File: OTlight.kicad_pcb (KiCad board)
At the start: 2 copper layers, 58 parts, among them P1 CONN_01X01, Q1 TEMT6000, Q2 Q_NMOS_GSD, T1 TRANSFO, U1 LM3478, U10 IN-14, U11 IN-14, U12 MAX6931, U13 IN-14, U14 MAX6920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

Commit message: Components fitted
Everything fits!
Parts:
- added C1: 220u, Capacitors_SMD:CP_Elec_6.3x7.7, F.Cu at (65.5, 127.6)
- added D1: STPS4S200, Diodes_SMD:D_SMB_Handsoldering, F.Cu at (48.3, 91.9)
- added U3: DS3231, BamboulabFootprints:DS3231, F.Cu at (128.5, 58.9)
- added U7: BME280, BamboulabFootprints:BME280, F.Cu at (98.1, 62.6)
- P1: footprint Connect:1pin -> Socket_Strips:Socket_Strip_Straight_1x01_Pitch2.54mm
- moved R24 202.0 mm to (54.9, 92.1), turned to 90 degrees
- moved C5 197.0 mm to (52.3, 128.0), turned to 270 degrees
- moved C6 193.8 mm to (78.5, 114.8)
- moved C4 189.6 mm to (58.9, 128.0), turned to 270 degrees
- moved R8 188.8 mm to (55.4, 128.0), turned to 270 degrees
- moved R1 188.7 mm to (79.8, 123.4)
- moved C2 187.9 mm to (65.0, 120.4), turned to 270 degrees
- moved R17 186.8 mm to (57.4, 92.3), turned to 270 degrees
- moved C3 182.9 mm to (74.7, 123.4)
- moved U1 182.1 mm to (74.2, 118.9), turned to 270 degrees
- moved R2 174.4 mm to (68.1, 120.4), turned to 270 degrees
- moved R4 170.3 mm to (94.0, 120.9), turned to 90 degrees
- moved R25 169.0 mm to (81.8, 91.4), turned to 90 degrees
- moved R28 168.9 mm to (97.5, 91.4), turned to 90 degrees
- moved R23 167.5 mm to (59.9, 91.9), turned to 90 degrees
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
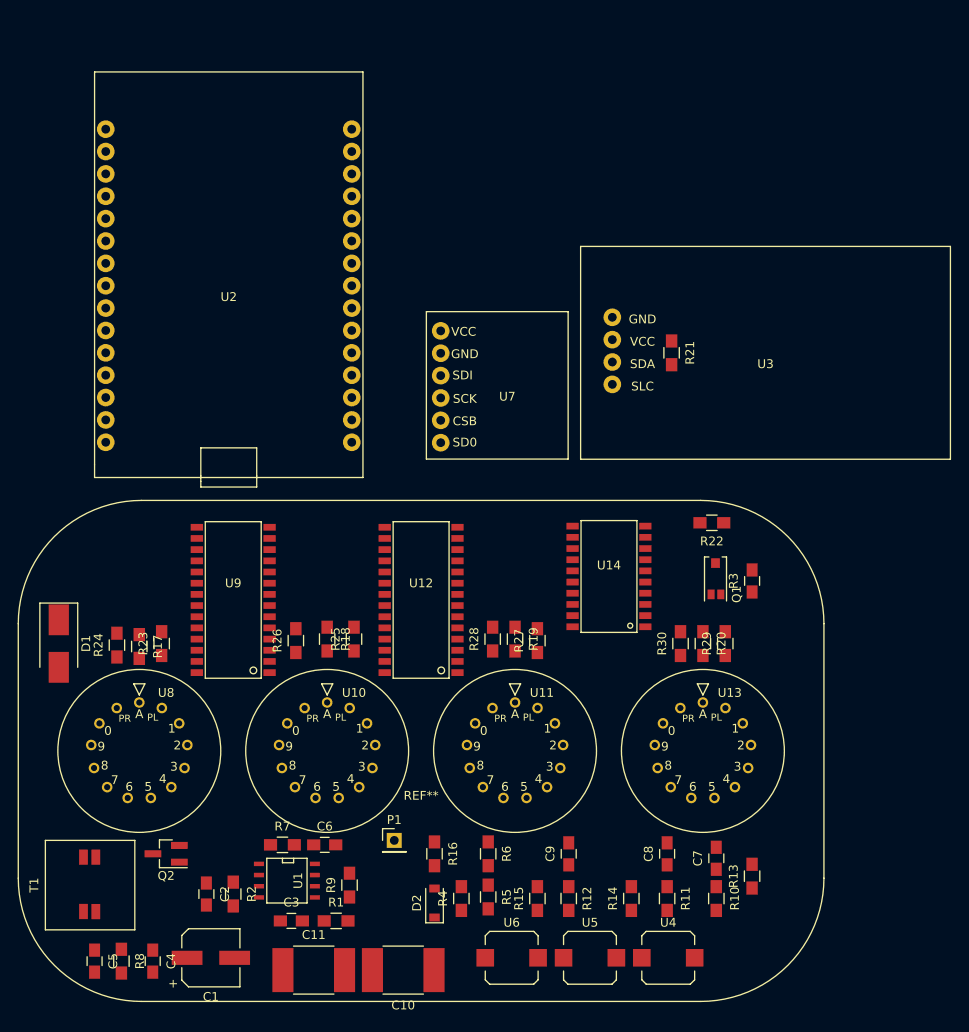
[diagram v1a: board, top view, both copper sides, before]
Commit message: PSU on board organised
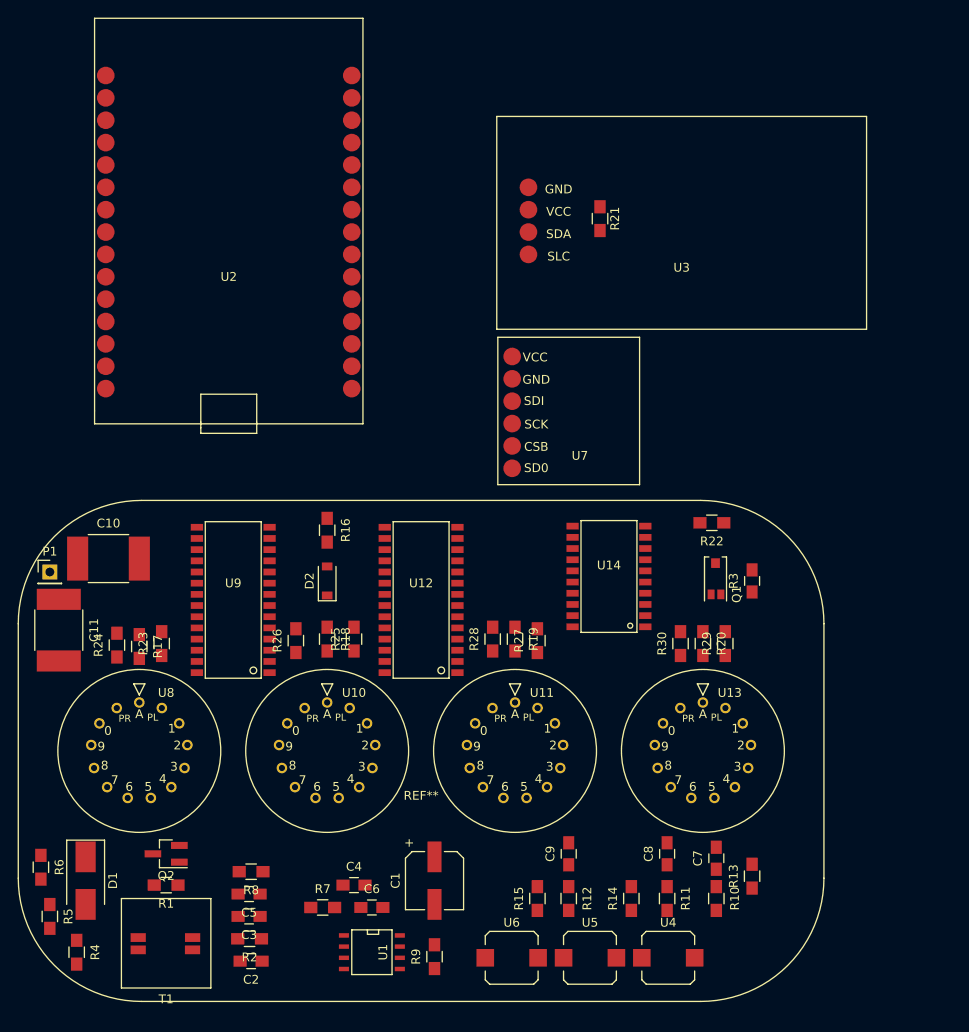
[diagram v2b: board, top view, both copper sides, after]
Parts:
- moved C10 57.5 mm to (53.9, 82.3), turned to 0 degrees
- moved R6 50.8 mm to (46.2, 117.3)
- moved R5 49.8 mm to (47.2, 122.9)
- moved P1 49.6 mm to (47.2, 83.8)
- moved C11 48.3 mm to (48.3, 90.4), turned to 270 degrees
- moved R4 44.1 mm to (50.3, 127.0), turned to 270 degrees
- moved R16 38.7 mm to (78.7, 79.1)
- moved D2 38.6 mm to (78.7, 84.8)
- moved D1 27.1 mm to (51.3, 118.9)
- moved C1 26.9 mm to (90.9, 118.9), turned to 270 degrees
- moved C4 24.4 mm to (81.8, 119.4), turned to 0 degrees
- moved R1 19.7 mm to (60.5, 119.4), turned to 180 degrees
- moved C5 19.1 mm to (69.9, 120.4), turned to 180 degrees
- moved R8 17.9 mm to (70.1, 117.9), turned to 180 degrees
- moved U3 17.6 mm to (119.0, 44.2)
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
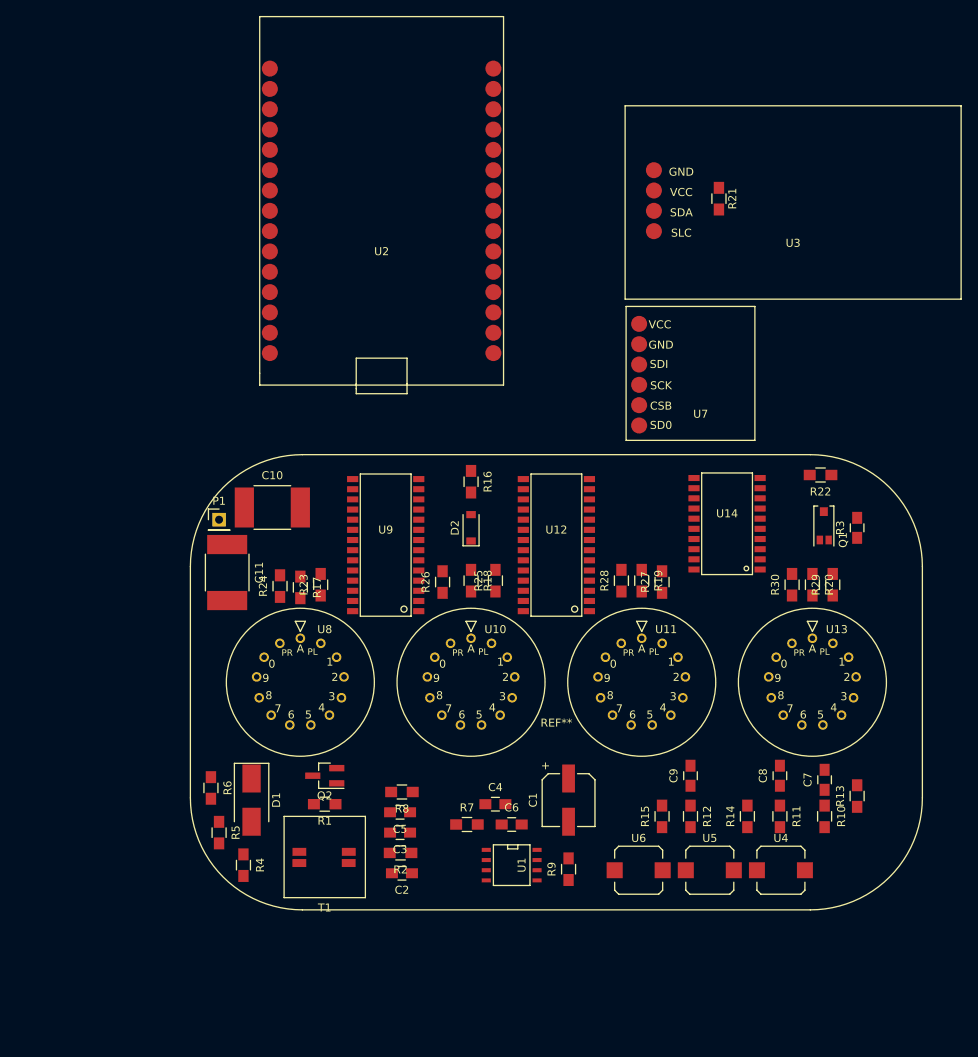
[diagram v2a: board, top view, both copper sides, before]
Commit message: ShiftRegisters + Nixies Routed
ESP in place also
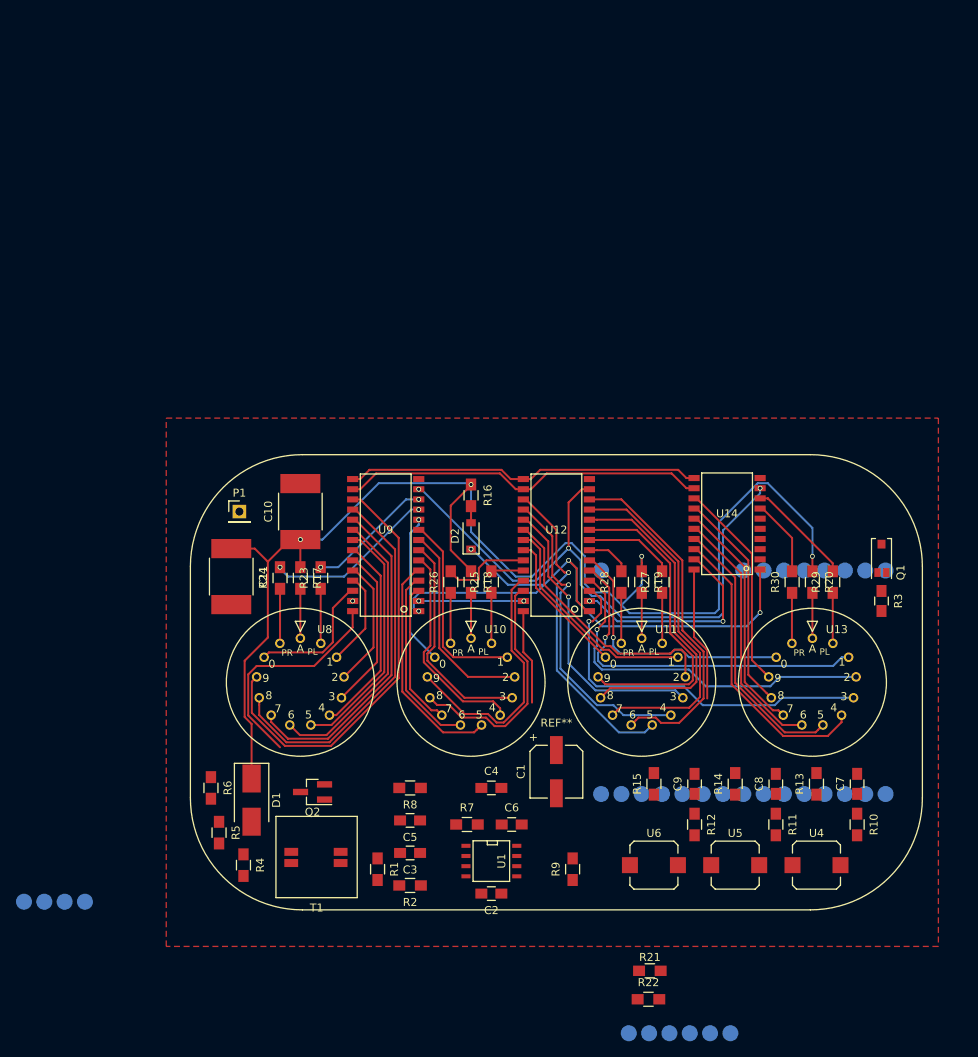
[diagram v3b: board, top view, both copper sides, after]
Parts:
- U2, U3, U7: moved to B.Cu
- moved U3 116.0 mm to (26.4, 114.2), turned to 90 degrees
- moved R21 96.9 mm to (101.1, 140.2), turned to 0 degrees
- moved U7 88.9 mm to (104.6, 154.4), turned to 270 degrees
- moved U2 74.3 mm to (112.8, 104.1), turned to 270 degrees
- moved R22 69.0 mm to (100.9, 143.8), turned to 0 degrees
- moved C2 11.5 mm to (81.3, 130.6)
- moved R1 10.5 mm to (67.1, 127.5), turned to 270 degrees
- moved R3 9.64 mm to (130.0, 94.0), turned to 270 degrees
- moved Q1 8.27 mm to (130.0, 90.4)
- moved R13 5.30 mm to (121.9, 116.8)
- moved U4 4.49 mm to (121.9, 127.0)
- moved R14 4.34 mm to (111.8, 116.8)
- moved R2 4.23 mm to (71.1, 129.5)
- moved R10 4.19 mm to (127.0, 121.9)
- moved R15 4.19 mm to (101.6, 116.8)
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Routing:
- net /HVout: track 0.00 -> 168.1 mm, vias 0 -> 4
- net Net-(D2-Pad1): track 0.00 -> 77.8 mm, vias 0 -> 4
- net /BLANK: track 0.00 -> 76.6 mm, vias 0 -> 3
- net +3V3: track 0.00 -> 57.0 mm
- net Net-(U8-Pad11): track 0.00 -> 53.6 mm
- net Net-(U12-Pad3): track 0.00 -> 47.6 mm, vias 0 -> 1
- net Net-(U8-Pad10): track 0.00 -> 47.2 mm
- net Net-(U12-Pad4): track 0.00 -> 46.2 mm, vias 0 -> 1
- net /LOAD: track 0.00 -> 45.9 mm
- net Net-(U12-Pad5): track 0.00 -> 45.5 mm, vias 0 -> 1
- net /CLK: track 0.00 -> 44.5 mm
- net Net-(U11-Pad8): track 0.00 -> 44.1 mm
- net Net-(U11-Pad9): track 0.00 -> 43.7 mm
- net Net-(U11-Pad10): track 0.00 -> 41.7 mm
- net Net-(U8-Pad9): track 0.00 -> 41.7 mm
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- added copper zone on F.Cu, net GND

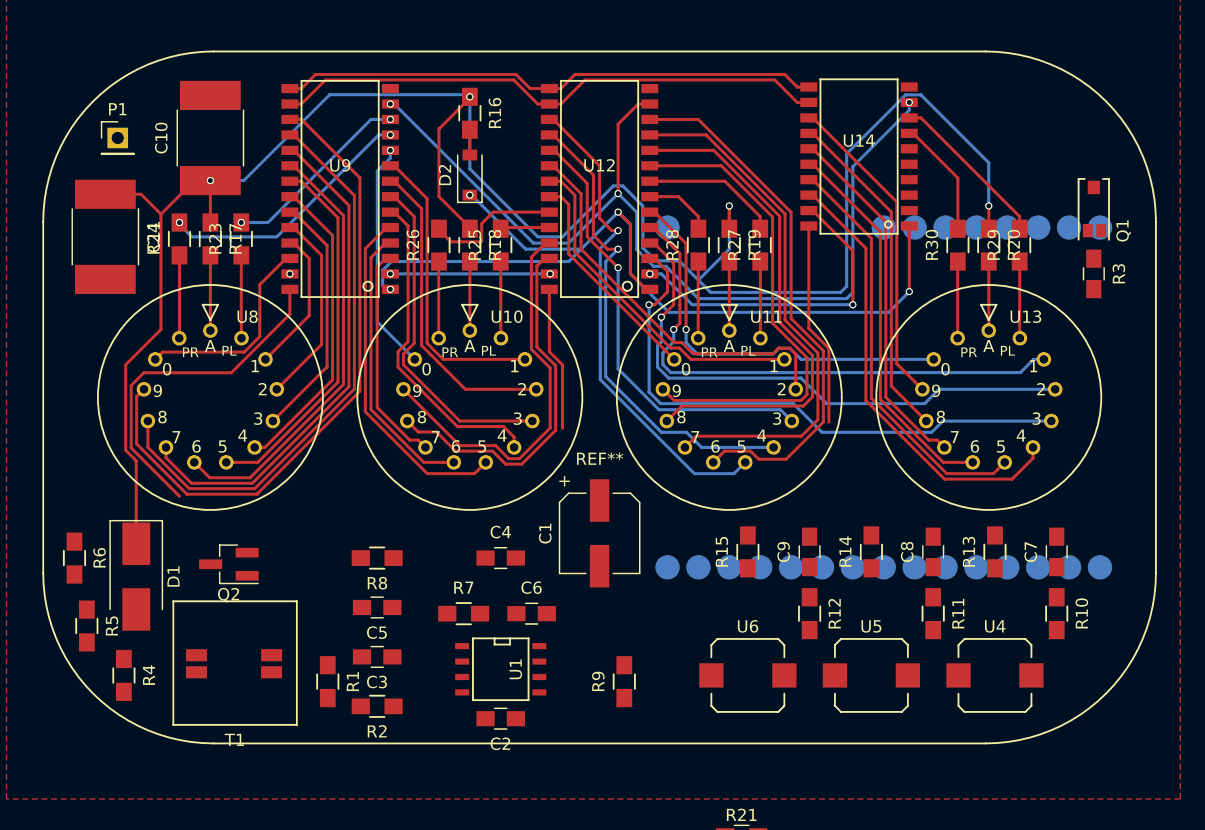
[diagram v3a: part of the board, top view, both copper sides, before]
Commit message: PSU rooted
Needs clean up and RTC+Barometer fitted
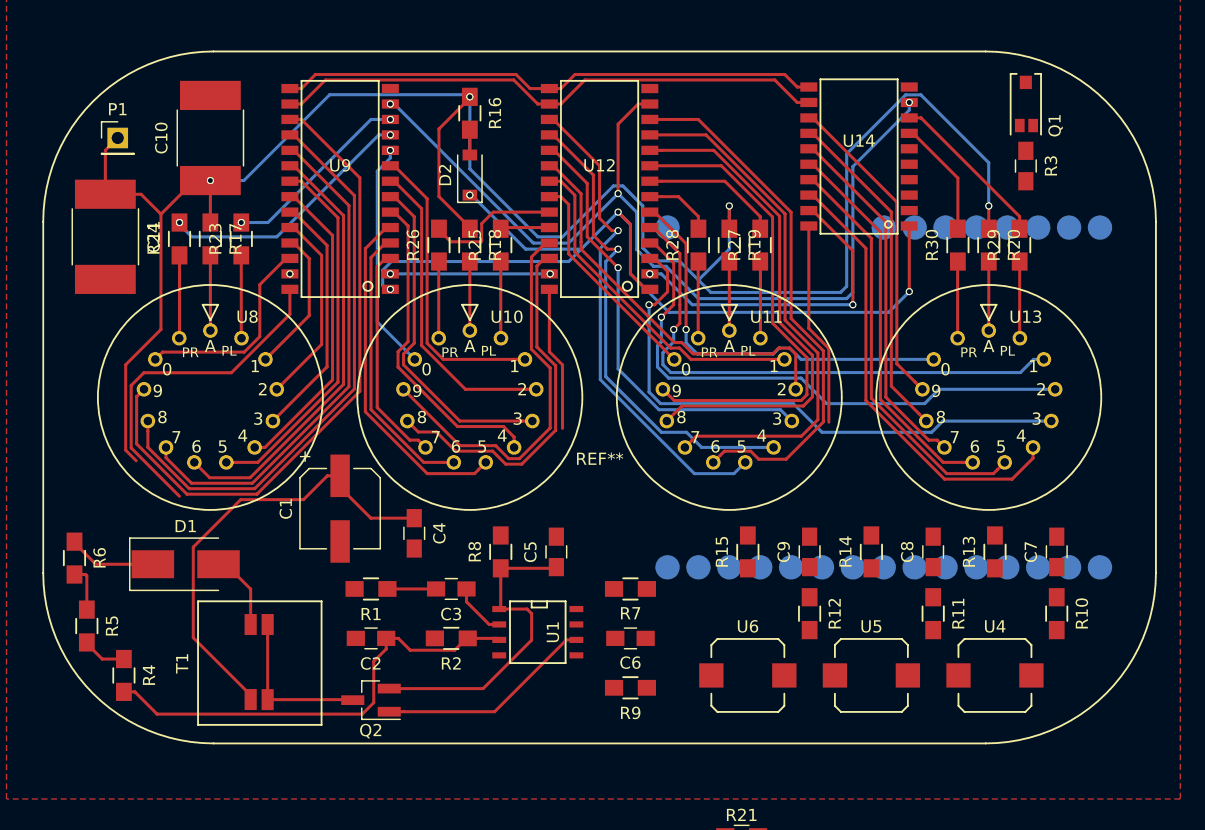
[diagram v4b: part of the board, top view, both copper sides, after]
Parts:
- moved C1 21.4 mm to (68.1, 113.3)
- moved Q2 16.2 mm to (70.6, 129.0)
- moved C5 15.4 mm to (85.9, 116.8), turned to 90 degrees
- moved R7 13.9 mm to (91.9, 119.9), turned to 180 degrees
- moved C2 12.5 mm to (70.6, 124.0)
- moved R3 10.5 mm to (124.5, 85.1)
- moved Q1 10.3 mm to (124.5, 81.8)
- moved R8 10.2 mm to (81.3, 116.8), turned to 90 degrees
- moved R1 8.41 mm to (70.6, 119.9), turned to 180 degrees
- moved C6 8.38 mm to (91.9, 124.0)
- moved C3 8.27 mm to (77.2, 119.9)
- moved R2 8.27 mm to (77.2, 124.0)
- moved C4 7.40 mm to (74.2, 115.3), turned to 270 degrees
- moved U1 4.31 mm to (84.3, 123.4)
- moved D1 4.19 mm to (55.4, 117.9), turned to 0 degrees
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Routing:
- net Net-(C2-Pad1): track 0.00 -> 37.6 mm
- net +5V: track 0.00 -> 37.1 mm
- net Net-(C5-Pad1): track 0.00 -> 26.1 mm
- net Net-(Q2-Pad1): track 0.00 -> 17.8 mm
- net Net-(Q2-Pad3): track 0.00 -> 13.2 mm
- net Net-(D1-Pad2): track 0.00 -> 6.40 mm
- net /HVout: track 168.1 -> 173.6 mm
- net Net-(C3-Pad1): track 0.00 -> 4.52 mm
- net Net-(C3-Pad2): track 0.00 -> 4.00 mm
- net Net-(R5-Pad1): track 0.00 -> 3.84 mm
- net Net-(R4-Pad1): track 0.00 -> 3.67 mm
